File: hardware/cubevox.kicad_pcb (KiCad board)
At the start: 4 copper layers, 200 x 150 mm, 223 parts, among them J1 USB-C, J101 J_IN NCJ6FA-H, J106 DC 9V, J108 OUT 6.35mm, J117 OLED SH1106, J3 TC2030-NL SWD, K101 G6K-2F-Y DC5, K102 G6K-2F-Y DC5, Q101 MMBT3904, SW101 ST-0-102 bat toggle, SW102 ST-0-102 bat toggle, SW103 ST-0-102 bat toggle, SW104 ST-0-102 bat toggle, SW105 ST-0-102 bat toggle, SW106 ST-0-102 bat toggle, SW107 ST-0-102 bat toggle, SW108 ST-0-102 bat toggle, U1 STM32H743VIT6, U101 CD74HC4067, U103 AP63205WU-7, U104 OPA2197IDR, U105 OPA2197IDR, U106 OPA2197IDR, U3 AP63203WU-7, U4 TLV75533PDBVR, U6 PCM5102APWR, U8 PCM1808PWR, Y1 25MHz 12pF

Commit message: layout: change on  (ledger 0153)
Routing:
- net /VIN_9V: track 154.6 -> 141.9 mm, vias 7 -> 4
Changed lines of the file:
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@@
-	)
-	(segment
-		(start 96.6 53.6)
-		(end 96.1 53.6)
-		(width 0.4)
-		(layer "F.Cu")
-		(net "/VIN_9V")
-	)
-	(segment
-		(start 93.85 54.55)
-		(end 93.85 55.05)
-		(width 0.4)
-		(layer "F.Cu")
-		(net "/VIN_9V")
 	)
 	(segment
 		(start 228.55 50.45)
 		(end 228 50.45)
-		(width 0.4)
-		(layer "F.Cu")
-		(net "/VIN_9V")
-	)
-	(segment
-		(start 233.5 50.25)
-		(end 233.5 49.75)
 		(width 0.4)
 		(layer "F.Cu")
@@
 	)
 	(via
-		(at 233.5 49.75)
-		(size 0.6)
-		(drill 0.3)
-		(layers "F.Cu" "B.Cu")
-		(net "/VIN_9V")
-	)
-	(via
-		(at 93.85 55.05)
-		(size 0.6)
-		(drill 0.3)
-		(layers "F.Cu" "B.Cu")
-		(net "/VIN_9V")
-	)
-	(via
 		(at 228 50.45)
-		(size 0.6)
-		(drill 0.3)
-		(layers "F.Cu" "B.Cu")
-		(net "/VIN_9V")
-	)
-	(via
-		(at 96.1 53.6)
 		(size 0.6)
 		(drill 0.3)
@@
 		(width 0.4)
 		(layer "B.Cu")
-		(net "/VIN_9V")
-	)
-	(segment
-		(start 98.15 55)
-		(end 96.75 53.6)
-		(width 0.4)
-		(layer "B.Cu")
-		(net "/VIN_9V")
-	)
-	(segment
-		(start 96.75 53.6)
-		(end 96.1 53.6)
-		(width 0.4)
-		(layer "B.Cu")
-		(net "/VIN_9V")
-	)
-	(segment
-		(start 94.65 55.05)
-		(end 93.85 55.05)
-		(width 0.4)
-		(layer "In2.Cu")
 		(net "/VIN_9V")
 	)
@@
 	(segment
 		(start 228 50.45)
-		(end 228.7 49.75)
-		(width 0.4)
-		(layer "In2.Cu")
-		(net "/VIN_9V")
-	)
-	(segment
-		(start 228 50.45)
 		(end 223.45 55)
 		(width 0.4)
@@
 		(start 105.75 51.15)
 		(end 103.25 53.65)
-		(width 0.4)
-		(layer "In2.Cu")
-		(net "/VIN_9V")
-	)
-	(segment
-		(start 228.7 49.75)
-		(end 233.5 49.75)
 		(width 0.4)
 		(layer "In2.Cu")
@@
 		(width 0.4)
 		(layer "In2.Cu")
-		(net "/VIN_9V")
-	)
-	(segment
-		(start 96.1 53.6)
-		(end 94.65 55.05)
-		(width 0.4)
-		(layer "In2.Cu")

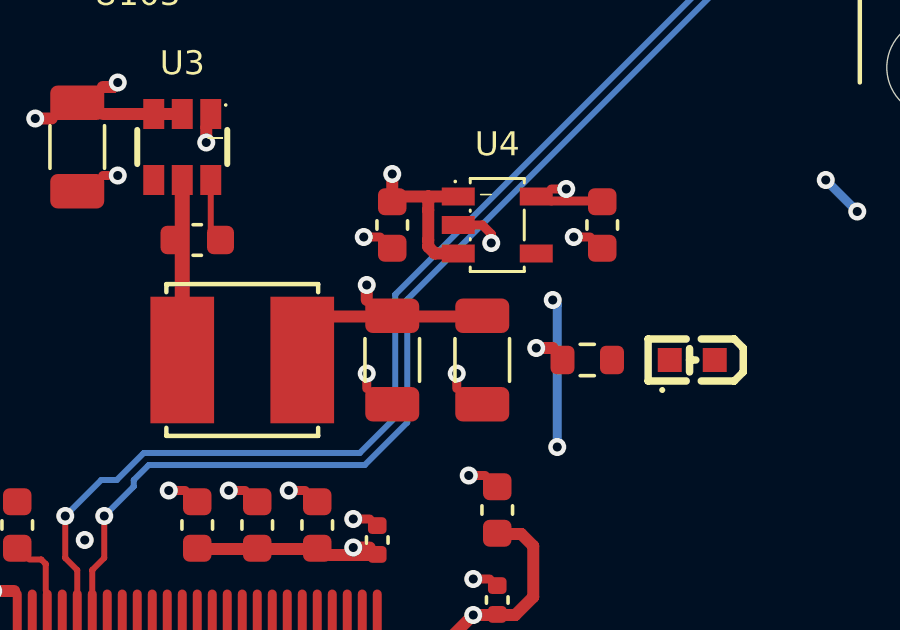
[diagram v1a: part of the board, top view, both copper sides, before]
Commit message: layout: change on /3V3 (ledger 0155)
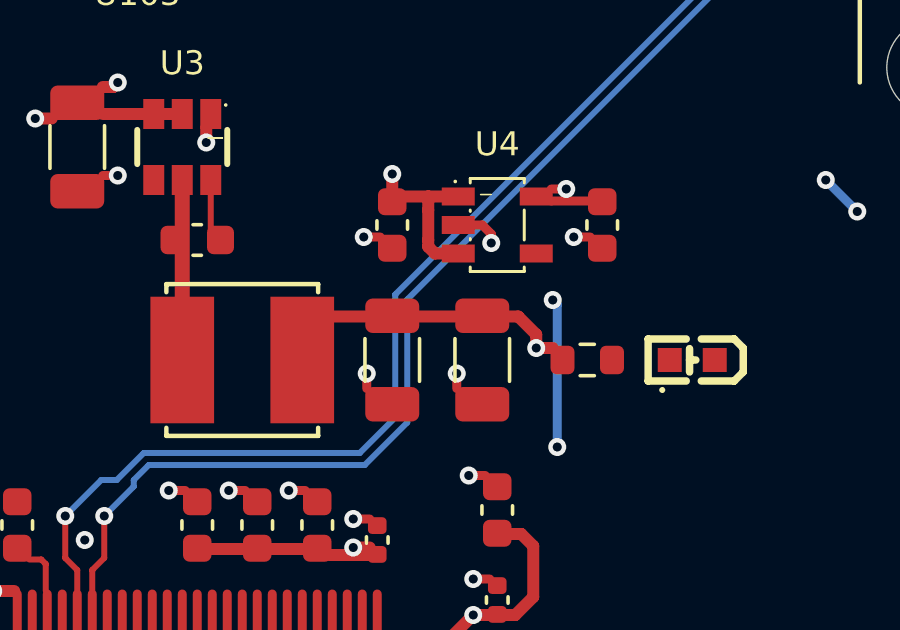
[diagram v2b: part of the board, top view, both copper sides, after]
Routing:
- net /3V3: track 616.6 -> 614.5 mm, vias 32 -> 31
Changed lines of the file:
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@@
+	)
+	(segment
+		(start 106.7 66.55)
+		(end 107.3 67.15)
+		(width 0.4)
+		(layer "F.Cu")
+		(net "/3V3")
 	)
 	(segment
@@
 	)
 	(segment
+		(start 106.1 66.55)
+		(end 106.7 66.55)
+		(width 0.4)
+		(layer "F.Cu")
+		(net "/3V3")
+	)
+	(segment
 		(start 89.1 75.7)
 		(end 88.5 75.1)
@@
 	)
 	(segment
-		(start 101.65 66)
-		(end 101.65 65.5)
-		(width 0.4)
-		(layer "F.Cu")
-		(net "/3V3")
-	)
-	(segment
 		(start 87.7 90.1)
 		(end 87.7 90.6)
@@
 		(start 232.15 123.8)
 		(end 231.6 123.8)
+		(width 0.4)
+		(layer "F.Cu")
+		(net "/3V3")
+	)
+	(segment
+		(start 107.3 67.15)
+		(end 107.3 67.6)
 		(width 0.4)
 		(layer "F.Cu")
@@
 	)
 	(via
-		(at 101.65 65.5)
-		(size 0.6)
-		(drill 0.3)
-		(layers "F.Cu" "B.Cu")
-		(net "/3V3")
-	)
-	(via
 		(at 96.3 60.75)
 		(size 0.6)
@@
 	)
 	(segment
+		(start 105.8 72.15)
+		(end 105.05 72.9)
+		(width 0.4)
+		(layer "In2.Cu")
+		(net "/3V3")
+	)
+	(segment
 		(start 93.15 96.55)
 		(end 93.15 99.2)
@@
 	)
 	(segment
-		(start 107.3 67.6)
-		(end 107.3 70.65)
-		(width 0.4)
-		(layer "In2.Cu")
-		(net "/3V3")
-	)
-	(segment
 		(start 94.85 59.3)
 		(end 93.85 59.3)
@@
 	)
 	(segment
+		(start 105.8 70.5)
+		(end 105.8 72.15)
+		(width 0.4)
+		(layer "In2.Cu")
+		(net "/3V3")
+	)
+	(segment
 		(start 105.1 88.8)
 		(end 104.45 89.45)
@@
 		(width 0.4)
 		(layer "In2.Cu")
-		(net "/3V3")
-	)
-	(segment
-		(start 107.3 70.65)
-		(end 105.05 72.9)
-		(width 0.4)
-		(layer "In2.Cu")

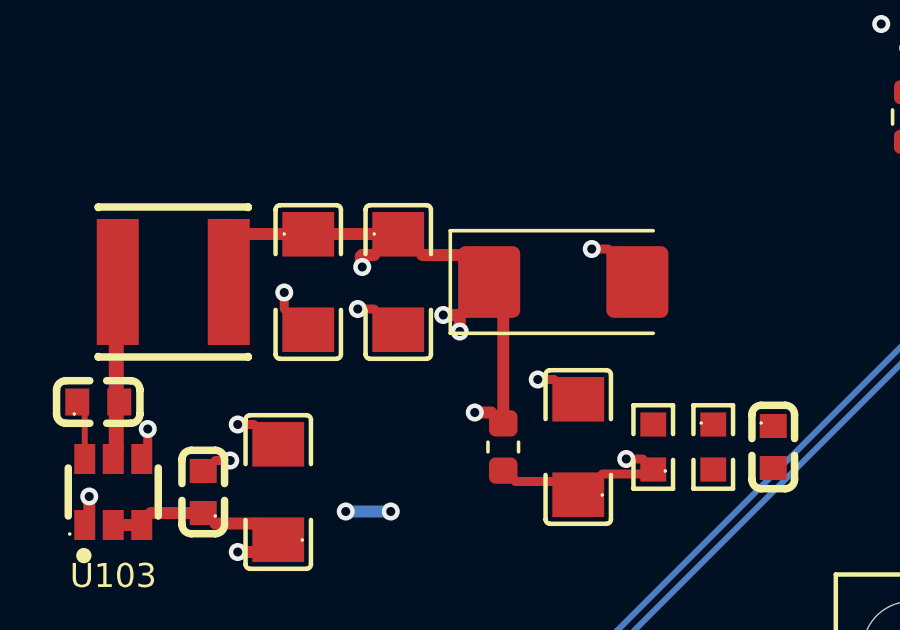
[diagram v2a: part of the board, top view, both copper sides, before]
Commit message: layout: change on /5V (ledger 0156)
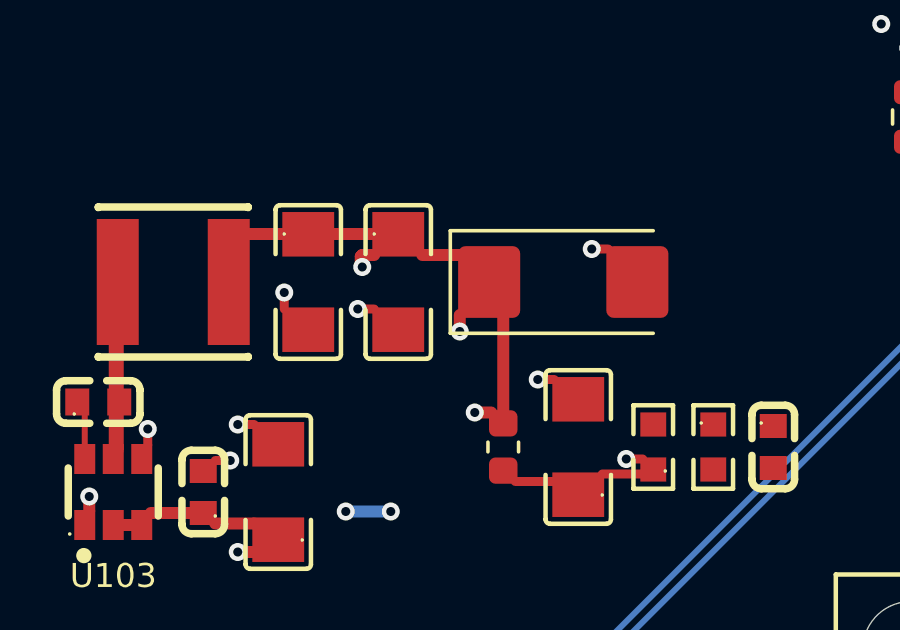
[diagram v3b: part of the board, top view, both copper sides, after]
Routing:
- net /5V: track 99.0 -> 98.7 mm, vias 9 -> 8
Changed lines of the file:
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@@
-	)
-	(segment
-		(start 105.55 47.1)
-		(end 105 47.1)
-		(width 0.4)
-		(layer "F.Cu")
-		(net "/5V")
 	)
 	(segment
@@
 	)
 	(via
-		(at 105 47.1)
-		(size 0.6)
-		(drill 0.3)
-		(layers "F.Cu" "B.Cu")
-		(net "/5V")
-	)
-	(via
 		(at 93.35 58.75)
 		(size 0.6)
@@
 	)
 	(segment
+		(start 105.55 47.65)
+		(end 104.45 47.65)
+		(width 0.4)
+		(layer "In2.Cu")
+		(net "/5V")
+	)
+	(segment
 		(start 102.3 45.5)
 		(end 94.65 53.15)
@@
 	)
 	(segment
-		(start 74.25 73.05)
-		(end 66.05 64.849999)
+		(start 104.45 47.65)
+		(end 93.35 58.75)
 		(width 0.4)
 		(layer "In2.Cu")
@@
 	)
 	(segment
-		(start 105 47.1)
-		(end 93.35 58.75)
+		(start 74.25 73.05)
+		(end 66.05 64.849999)
 		(width 0.4)
 		(layer "In2.Cu")

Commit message: layout: change on  (ledger 0157)
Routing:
- net /h7core_block/ADC_VCC: track 30.7 -> 17.5 mm, vias 3 -> 0
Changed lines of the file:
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@@
-	)
-	(segment
-		(start 135.6 98.5)
-		(end 135.05 98.5)
-		(width 0.3)
-		(layer "F.Cu")
-		(net "/h7core_block/ADC_VCC")
-	)
-	(segment
-		(start 128.85 104.3)
-		(end 128.25 104.9)
-		(width 0.3)
-		(layer "F.Cu")
-		(net "/h7core_block/ADC_VCC")
 	)
 	(segment
@@
 	)
 	(segment
-		(start 132.75 102.35)
-		(end 132.75 102.85)
-		(width 0.3)
-		(layer "F.Cu")
-		(net "/h7core_block/ADC_VCC")
-	)
-	(segment
-		(start 128.85 103.9)
-		(end 128.85 104.3)
-		(width 0.3)
-		(layer "F.Cu")
-		(net "/h7core_block/ADC_VCC")
-	)
-	(segment
 		(start 135.6 99.15)
 		(end 134.65 99.15)
@@
 		(net "/h7core_block/ADC_VCC")
 	)
-	(segment
-		(start 128.25 104.9)
-		(end 128.15 104.9)
-		(width 0.3)
-		(layer "F.Cu")
-		(net "/h7core_block/ADC_VCC")
-	)
-	(via
-		(at 135.05 98.5)
-		(size 0.6)
-		(drill 0.3)
-		(layers "F.Cu" "B.Cu")
-		(net "/h7core_block/ADC_VCC")
-	)
-	(via
-		(at 128.15 104.9)
-		(size 0.6)
-		(drill 0.3)
-		(layers "F.Cu" "B.Cu")
-		(net "/h7core_block/ADC_VCC")
-	)
-	(via
-		(at 132.75 102.85)
-		(size 0.6)
-		(drill 0.3)
-		(layers "F.Cu" "B.Cu")
-		(net "/h7core_block/ADC_VCC")
-	)
-	(segment
-		(start 130.199999 102.85)
-		(end 132.75 102.85)
-		(width 0.3)
-		(layer "B.Cu")
-		(net "/h7core_block/ADC_VCC")
-	)
-	(segment
-		(start 128.15 104.9)
-		(end 130.199999 102.85)
-		(width 0.3)
-		(layer "B.Cu")
-		(net "/h7core_block/ADC_VCC")
-	)
-	(segment
-		(start 132.75 102.85)
-		(end 135.05 100.55)
-		(width 0.3)
-		(layer "In2.Cu")
-		(net "/h7core_block/ADC_VCC")
-	)
-	(segment
-		(start 135.05 100.55)
-		(end 135.05 98.5)
-		(width 0.3)
-		(layer "In2.Cu")
-		(net "/h7core_block/ADC_VCC")
-	)

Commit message: layout: change on /3V3 (ledger 0158)
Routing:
- net /3V3: track 614.5 -> 612.4 mm
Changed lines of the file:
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@@
-	)
-	(segment
-		(start 87.7 90.6)
-		(end 83.2 90.6)
-		(width 0.4)
-		(layer "In2.Cu")
-		(net "/3V3")
-	)
-	(segment
-		(start 105.8 70.5)
-		(end 107.65 72.35)
-		(width 0.4)
-		(layer "In2.Cu")
-		(net "/3V3")
-	)
-	(segment
-		(start 101.65 65.5)
-		(end 100.45 66.7)
-		(width 0.4)
-		(layer "In2.Cu")
-		(net "/3V3")
 	)
 	(segment
@@
 	)
 	(segment
-		(start 82.55 91.25)
-		(end 82.55 93.85)
-		(width 0.4)
-		(layer "In2.Cu")
-		(net "/3V3")
-	)
-	(segment
 		(start 89.2 75.7)
 		(end 87.75 74.25)
@@
 	)
 	(segment
+		(start 93.15 95.9)
+		(end 93.15 99.2)
+		(width 0.4)
+		(layer "In2.Cu")
+		(net "/3V3")
+	)
+	(segment
 		(start 134.5 57.75)
 		(end 136.9 60.15)
@@
 	)
 	(segment
+		(start 93.15 95.9)
+		(end 93.75 95.9)
+		(width 0.4)
+		(layer "In2.Cu")
+		(net "/3V3")
+	)
+	(segment
 		(start 105.05 72.9)
 		(end 105.05 73.4)
@@
 	)
 	(segment
-		(start 82.55 80.35)
-		(end 82.55 91.25)
+		(start 98.4 65.5)
+		(end 100.45 65.5)
+		(width 0.4)
+		(layer "In2.Cu")
+		(net "/3V3")
+	)
+	(segment
+		(start 107.3 72)
+		(end 107.65 72.35)
 		(width 0.4)
 		(layer "In2.Cu")
@@
 	)
 	(segment
-		(start 92.5 95.9)
-		(end 93.15 96.55)
+		(start 84.6 95.9)
+		(end 93.15 95.9)
+		(width 0.4)
+		(layer "In2.Cu")
+		(net "/3V3")
+	)
+	(segment
+		(start 100.45 65.5)
+		(end 100.45 73.6)
 		(width 0.4)
 		(layer "In2.Cu")
@@
 	)
 	(segment
-		(start 92.5 95.9)
-		(end 93.75 95.9)
+		(start 106.65 71.3)
+		(end 105.05 72.9)
 		(width 0.4)
 		(layer "In2.Cu")
@@
 	)
 	(segment
-		(start 83.2 90.6)
-		(end 82.55 91.25)
-		(width 0.4)
-		(layer "In2.Cu")
-		(net "/3V3")
-	)
-	(segment
 		(start 92.3 144.45)
 		(end 92.3 149.95)
@@
 	)
 	(segment
+		(start 82.55 90.6)
+		(end 82.55 93.85)
+		(width 0.4)
+		(layer "In2.Cu")
+		(net "/3V3")
+	)
+	(segment
 		(start 159.6 123.8)
 		(end 183.6 123.8)
@@
 	)
 	(segment
+		(start 107.3 71.3)
+		(end 106.65 71.3)
+		(width 0.4)
+		(layer "In2.Cu")
+		(net "/3V3")
+	)
+	(segment
 		(start 87.6 123.8)
 		(end 63.6 123.8)
@@
 	)
 	(segment
-		(start 105.8 72.15)
-		(end 105.05 72.9)
-		(width 0.4)
-		(layer "In2.Cu")
-		(net "/3V3")
-	)
-	(segment
-		(start 93.15 96.55)
-		(end 93.15 99.2)
-		(width 0.4)
-		(layer "In2.Cu")
-		(net "/3V3")
-	)
-	(segment
-		(start 101.65 65.5)
+		(start 100.45 65.5)
 		(end 104.65 65.5)
 		(width 0.4)
@@
 	)
 	(segment
-		(start 98.4 65.5)
-		(end 101.65 65.5)
-		(width 0.4)
-		(layer "In2.Cu")
-		(net "/3V3")
-	)
-	(segment
 		(start 136.9 60.15)
 		(end 149.05 60.15)
@@
 	)
 	(segment
-		(start 100.45 66.7)
-		(end 100.45 73.6)
-		(width 0.4)
-		(layer "In2.Cu")
-		(net "/3V3")
-	)
-	(segment
 		(start 125.25 102.5)
 		(end 125.5 102.5)
@@
 	)
 	(segment
-		(start 107.3 67.6)
-		(end 105.8 69.1)
-		(width 0.4)
-		(layer "In2.Cu")
-		(net "/3V3")
-	)
-	(segment
-		(start 105.8 69.1)
-		(end 105.8 70.5)
-		(width 0.4)
-		(layer "In2.Cu")
-		(net "/3V3")
-	)
-	(segment
 		(start 125.5 102.5)
 		(end 126.9 102.5)
@@
 	)
 	(segment
-		(start 84.6 95.9)
-		(end 92.5 95.9)
+		(start 107.3 67.6)
+		(end 107.3 71.3)
 		(width 0.4)
 		(layer "In2.Cu")
@@
 	)
 	(segment
+		(start 82.55 80.35)
+		(end 82.55 90.6)
+		(width 0.4)
+		(layer "In2.Cu")
+		(net "/3V3")
+	)
+	(segment
+		(start 107.3 71.3)
+		(end 107.3 72)
+		(width 0.4)
+		(layer "In2.Cu")
+		(net "/3V3")
+	)
+	(segment
 		(start 134.5 57.8)
 		(end 134.5 57.75)
@@
 	)
 	(segment
-		(start 105.8 70.5)
-		(end 105.8 72.15)
-		(width 0.4)
-		(layer "In2.Cu")
-		(net "/3V3")
-	)
-	(segment
 		(start 105.1 88.8)
 		(end 104.45 89.45)
 		(width 0.4)
 		(layer "In2.Cu")
+		(net "/3V3")
+	)
+	(segment
+		(start 87.7 90.6)
+		(end 82.55 90.6)
+		(width 0.4)
+		(layer "In2.Cu")

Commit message: layout: change on /3V3 (ledger 0159)
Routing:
- net /3V3: track 612.4 -> 613.4 mm
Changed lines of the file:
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@@
-	)
-	(segment
-		(start 93.15 95.9)
-		(end 93.15 99.2)
-		(width 0.4)
-		(layer "In2.Cu")
-		(net "/3V3")
 	)
 	(segment
@@
 	)
 	(segment
+		(start 87.3 91)
+		(end 87.7 90.6)
+		(width 0.4)
+		(layer "In2.Cu")
+		(net "/3V3")
+	)
+	(segment
 		(start 93.8 99.85)
 		(end 77.35 99.85)
@@
 	)
 	(segment
+		(start 93.15 96.8)
+		(end 93.55 97.2)
+		(width 0.4)
+		(layer "In2.Cu")
+		(net "/3V3")
+	)
+	(segment
 		(start 134.5 57.75)
 		(end 136.1 56.15)
@@
 	)
 	(segment
-		(start 100.45 65.5)
-		(end 100.45 73.6)
-		(width 0.4)
-		(layer "In2.Cu")
-		(net "/3V3")
-	)
-	(segment
 		(start 104.45 75.6)
 		(end 104.45 75.75)
@@
 	)
 	(segment
+		(start 93.15 95.9)
+		(end 93.15 96.8)
+		(width 0.4)
+		(layer "In2.Cu")
+		(net "/3V3")
+	)
+	(segment
 		(start 207.6 123.8)
 		(end 231.6 123.8)
@@
 	)
 	(segment
+		(start 93.55 97.2)
+		(end 93.55 98)
+		(width 0.4)
+		(layer "In2.Cu")
+		(net "/3V3")
+	)
+	(segment
 		(start 107.6 88.8)
 		(end 105.1 88.8)
@@
 	)
 	(segment
+		(start 100.85 66.8)
+		(end 100.85 67.2)
+		(width 0.4)
+		(layer "In2.Cu")
+		(net "/3V3")
+	)
+	(segment
 		(start 106.65 71.3)
 		(end 105.05 72.9)
@@
 	)
 	(segment
+		(start 83.45 90.6)
+		(end 83.85 91)
+		(width 0.4)
+		(layer "In2.Cu")
+		(net "/3V3")
+	)
+	(segment
 		(start 92.3 144.45)
 		(end 92.3 149.95)
@@
 	)
 	(segment
+		(start 100.45 67.6)
+		(end 100.45 73.6)
+		(width 0.4)
+		(layer "In2.Cu")
+		(net "/3V3")
+	)
+	(segment
 		(start 117.25 62.75)
 		(end 119.7 60.3)
@@
 	)
 	(segment
+		(start 100.45 66.4)
+		(end 100.85 66.8)
+		(width 0.4)
+		(layer "In2.Cu")
+		(net "/3V3")
+	)
+	(segment
 		(start 82.55 90.6)
 		(end 82.55 93.85)
@@
 	)
 	(segment
+		(start 93.15 98.4)
+		(end 93.15 99.2)
+		(width 0.4)
+		(layer "In2.Cu")
+		(net "/3V3")
+	)
+	(segment
 		(start 136.1 56.15)
 		(end 136.1 55.75)
@@
 	)
 	(segment
+		(start 100.45 65.5)
+		(end 100.45 66.4)
+		(width 0.4)
+		(layer "In2.Cu")
+		(net "/3V3")
+	)
+	(segment
 		(start 88.6 153.65)
 		(end 64.599999 153.65)
@@
 	)
 	(segment
+		(start 83.85 91)
+		(end 87.3 91)
+		(width 0.4)
+		(layer "In2.Cu")
+		(net "/3V3")
+	)
+	(segment
 		(start 116.65 62.75)
 		(end 117.25 62.75)
@@
 	)
 	(segment
+		(start 100.85 67.2)
+		(end 100.45 67.6)
+		(width 0.4)
+		(layer "In2.Cu")
+		(net "/3V3")
+	)
+	(segment
 		(start 125.5 102.5)
 		(end 126.9 102.5)
@@
 	)
 	(segment
+		(start 82.55 90.6)
+		(end 83.45 90.6)
+		(width 0.4)
+		(layer "In2.Cu")
+		(net "/3V3")
+	)
+	(segment
 		(start 82.55 80.35)
 		(end 82.55 90.6)
@@
 	)
 	(segment
-		(start 87.7 90.6)
-		(end 82.55 90.6)
-		(width 0.4)
-		(layer "In2.Cu")
-		(net "/3V3")
-	)
-	(segment
 		(start 87.6 123.8)
 		(end 88.6 124.8)
@@
 		(width 0.4)
 		(layer "In2.Cu")
+		(net "/3V3")
+	)
+	(segment
+		(start 93.55 98)
+		(end 93.15 98.4)
+		(width 0.4)
+		(layer "In2.Cu")

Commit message: layout: change on /3V3A (ledger 0160)
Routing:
- net /3V3A: vias 14 -> 13
- net /9V_JACK: vias 2 -> 1
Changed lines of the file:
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@@
-	)
-	(segment
-		(start 186.2 144.7)
-		(end 186.15 144.7)
-		(width 0.3)
-		(layer "F.Cu")
-		(net "/3V3A")
 	)
 	(segment
@@
 	)
 	(via
-		(at 186.15 144.7)
-		(size 0.6)
-		(drill 0.3)
-		(layers "F.Cu" "B.Cu")
-		(net "/3V3A")
-	)
-	(via
 		(at 196.3 152.1)
 		(size 0.6)
@@
 	)
 	(segment
-		(start 185.45 144)
-		(end 186.15 144.7)
-		(width 0.3)
-		(layer "In2.Cu")
-		(net "/3V3A")
-	)
-	(segment
 		(start 188.3 146.8)
 		(end 188.3 152.1)
@@
 	)
 	(segment
+		(start 185.45 144)
+		(end 186.95 145.5)
+		(width 0.3)
+		(layer "In2.Cu")
+		(net "/3V3A")
+	)
+	(segment
 		(start 139 145.5)
 		(end 140.25 144.25)
@@
 		(start 108.25 72.1)
 		(end 108.25 90)
-		(width 0.3)
-		(layer "In2.Cu")
-		(net "/3V3A")
-	)
-	(segment
-		(start 186.15 144.7)
-		(end 186.95 145.5)
 		(width 0.3)
 		(layer "In2.Cu")
@@
 	)
 	(segment
-		(start 233.6 35.25)
-		(end 233.55 35.25)
-		(width 0.4)
-		(layer "F.Cu")
-		(net "/9V_JACK")
-	)
-	(segment
 		(start 233.5 47.75)
 		(end 233.5 48.25)
@@
 		(size 0.6)
 		(drill 0.3)
-		(layers "F.Cu" "B.Cu")
-		(net "/9V_JACK")
-	)
-	(via
-		(at 233.55 35.25)
-		(size 0.6)
-		(drill 0.3)

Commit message: layout: change on /3V3A,/9V_JACK (ledger 0161)
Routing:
- net /3V3A: vias 13 -> 14
- net /9V_JACK: vias 1 -> 2
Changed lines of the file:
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@@
+	)
+	(segment
+		(start 186.2 144.7)
+		(end 186.15 144.7)
+		(width 0.3)
+		(layer "F.Cu")
+		(net "/3V3A")
 	)
 	(segment
@@
 	)
 	(via
+		(at 186.15 144.7)
+		(size 0.6)
+		(drill 0.3)
+		(layers "F.Cu" "B.Cu")
+		(net "/3V3A")
+	)
+	(via
 		(at 100.05 98.4)
 		(size 0.6)
@@
 	)
 	(segment
+		(start 185.45 144)
+		(end 186.15 144.7)
+		(width 0.3)
+		(layer "In2.Cu")
+		(net "/3V3A")
+	)
+	(segment
 		(start 108.25 90)
 		(end 107.65 90.6)
@@
 	)
 	(segment
+		(start 186.15 144.7)
+		(end 186.95 145.5)
+		(width 0.3)
+		(layer "In2.Cu")
+		(net "/3V3A")
+	)
+	(segment
 		(start 188.3 146.8)
 		(end 188.3 152.1)
-		(width 0.3)
-		(layer "In2.Cu")
-		(net "/3V3A")
-	)
-	(segment
-		(start 185.45 144)
-		(end 186.95 145.5)
 		(width 0.3)
 		(layer "In2.Cu")
@@
 	)
 	(segment
+		(start 233.6 35.25)
+		(end 233.55 35.25)
+		(width 0.4)
+		(layer "F.Cu")
+		(net "/9V_JACK")
+	)
+	(segment
 		(start 233.5 47.75)
 		(end 233.5 48.25)
@@
 		(net "/9V_JACK")
 	)
+	(via
+		(at 233.55 35.25)
+		(size 0.6)
+		(drill 0.3)
+		(layers "F.Cu" "B.Cu")
+		(net "/9V_JACK")
+	)
